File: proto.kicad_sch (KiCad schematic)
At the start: 0 parts

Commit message: update pcb and schematic
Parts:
- added C1, C10, C11, C12, C2, C6: 10uF, Capacitor_SMD:C_0603_1608Metric_Pad1.08x0.95mm_HandSolder, symbol Device:C
- added C13, C14, C15: 0.1uF, Capacitor_SMD:C_0201_0603Metric_Pad0.64x0.40mm_HandSolder, symbol Device:C
- added C3, C8, C9: 4.7uF, Capacitor_SMD:C_0603_1608Metric_Pad1.08x0.95mm_HandSolder, symbol Device:C
- added C4, C5: 220uF, Capacitor_THT:CP_Radial_D10.0mm_P3.80mm, symbol Device:C_Polarized
- added C7: 1uF, Capacitor_SMD:C_0402_1005Metric_Pad0.74x0.62mm_HandSolder, symbol Device:C
- added D1: LED_RGBA, LED_SMD:LED_RGB_Wuerth-PLCC4_3.2x2.8mm_150141M173100, symbol Device:LED_RGBA
- added IC1: WM8960CGEFL_V, WM8960CGEFL_V:QFN50P500X500X100-33N, symbol WM8960CGEFL_V:WM8960CGEFL_V
- added J1: Micro_SD_Card, Connector_Card:microSD_HC_Wuerth_693072010801, symbol Connector:Micro_SD_Card
- added J10: CS, xiao_esp32c3_model:Untitled, symbol Connector:Conn_01x01_Socket
- added J11: BL, xiao_esp32c3_model:Untitled, symbol Connector:Conn_01x01_Socket
- added J12: BAT+, xiao_esp32c3_model:Untitled, symbol Connector:Conn_01x01_Socket
- added J13: BAT-, xiao_esp32c3_model:Untitled, symbol Connector:Conn_01x01_Socket
- added J14: L-, xiao_esp32c3_model:Untitled, symbol Connector:Conn_01x01_Socket
- added J15: L+, xiao_esp32c3_model:Untitled, symbol Connector:Conn_01x01_Socket
- added J16: R-, xiao_esp32c3_model:Untitled, symbol Connector:Conn_01x01_Socket
- added J17: R+, xiao_esp32c3_model:Untitled, symbol Connector:Conn_01x01_Socket
- added J2: AudioJack3, Connector_Audio:Jack_3.5mm_Lumberg_1503_02_Horizontal, symbol Connector_Audio:AudioJack3
- added J3: USB_C_Receptacle_PowerOnly_6P, Connector_USB:USB_C_Receptacle_GCT_USB4125-xx-x-0190_6P_TopMnt_Horizontal, symbol Connector:USB_C_Receptacle_PowerOnly_6P
- added J4: GND, xiao_esp32c3_model:Untitled, symbol Connector:Conn_01x01_Socket
- added J5: VCC, xiao_esp32c3_model:Untitled, symbol Connector:Conn_01x01_Socket
- added J6: SCL, xiao_esp32c3_model:Untitled, symbol Connector:Conn_01x01_Socket
- added J7: SDA, xiao_esp32c3_model:Untitled, symbol Connector:Conn_01x01_Socket
- added J8: RES, xiao_esp32c3_model:Untitled, symbol Connector:Conn_01x01_Socket
- added J9: DC, xiao_esp32c3_model:Untitled, symbol Connector:Conn_01x01_Socket
- added R1, R2: 5.1k, Resistor_SMD:R_0201_0603Metric_Pad0.64x0.40mm_HandSolder, symbol Device:R
- added R3: 2k, Resistor_SMD:R_0201_0603Metric_Pad0.64x0.40mm_HandSolder, symbol Device:R
- added R4: 8k, Resistor_SMD:R_0201_0603Metric_Pad0.64x0.40mm_HandSolder, symbol Device:R
- added R5: 1.5k, Resistor_SMD:R_0201_0603Metric_Pad0.64x0.40mm_HandSolder, symbol Device:R
- added R6, R7, R8, R9: 10k, Resistor_SMD:R_0201_0603Metric_Pad0.64x0.40mm_HandSolder, symbol Device:R
- added SW1, SW2, SW3, SW4, SW5, SW6, SW7, SW8: SW_Push, Button_Switch_THT:SW_PUSH_6mm, symbol Switch:SW_Push
- added TH1: Thermistor, Resistor_SMD:R_0402_1005Metric_Pad0.72x0.64mm_HandSolder, symbol Device:Thermistor
- added U1: (no value), pico2:Raspberrypi pico2 THT, symbol Raspberrypi pico2 W:U
- added U2: BQ24074RGT, Package_DFN_QFN:VQFN-16-1EP_3x3mm_P0.5mm_EP1.6x1.6mm, symbol Battery_Management:BQ24074RGT
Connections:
- new net: J3.A5 (CC1), R2.2
- new net: C4.2, J2.R, R9.2
- new net: IC1.23 (SPK_LN), J14.1 (Pin_1)
- new net: C3.1, IC1.27 (VMID)
- new net: R5.1, U2.12 (ILIM)
- new net: IC1.19 (SPK_RN), J16.1 (Pin_1)
- new net: IC1.22 (SPK_RP), J17.1 (Pin_1)
- new net: IC1.25 (SPK_LP), J15.1 (Pin_1)
- new net: C4.1, IC1.29 (HP_R)
- new net: C5.1, IC1.31 (HP_L)
- new net: C5.2, J2.T, R8.2
- new net: C7.1, J3.A9 (VBUS), J3.B9 (VBUS), U2.13 (IN)
- new net: R4.1, U2.15 (ITERM)
- new net: R3.1, U2.16 (ISET)
- new net: R7.2, U2.7 (~{PGOOD})
- new net: R6.1, U2.9 (~{CHG})
- new net: J3.B5 (CC2), R1.2
- new net +3.3V: C1.1, C10.2, C13.2, C2.1, C6.1, IC1.10 (DBVDD), IC1.32 (AVDD), IC1.8 (DCVDD), J1.4 (VDD), J11.1 (Pin_1), J5.1 (Pin_1), R6.2, R7.1, U1.36 (3V3_OUT), U1.37 (3V3_EN)
- new net +5V: C11.2, C12.2, C14.2, C15.2, IC1.21 (SPKVDD2), IC1.26 (SPKVDD1), U1.40 (VBUS), U2.6 (EN1)
- new net B: D1.3 (BK), U1.29 (GP22)
- new net BAT+: C9.1, J12.1 (Pin_1), U2.2 (BAT), U2.3 (BAT)
- new net BAT-: J13.1 (Pin_1), TH1.1
- new net BLCK: IC1.12 (BCLK), U1.32 (GP27/ADC1/I2C1_SCL)
- new net CS: J1.2 (DAT3/CD), J10.1 (Pin_1), U1.1 (GP0/I2C0_SDA/UART0_TX), U1.17 (GP13/SPI1_CSn/I2C0_SCL/UART0_RX)
- new net DACDAT: IC1.14 (DACDAT), U1.19 (GP14/SPI1_SCK/I2C1_SCL)
- new net DACLRC: IC1.13 (DACLRC), U1.20 (GP15/SPI1_TX/I2C1_SCL)
- new net DC: J9.1 (Pin_1), U1.2 (GP1_/I2C0_SCL/UART0_RX)
- new net G: D1.2 (GK), U1.34 (GP28/ADC2)
- new net GND: C1.2, C10.1, C11.1, C12.1, C13.1, C14.1, C15.1, C2.2, C3.2, C6.2, C7.2, C8.2, C9.2, D1.4 (A), IC1.20 (SPKGND2), IC1.24 (SPKGND1), IC1.28 (AGND), IC1.33 (GND_PADDLE), IC1.9 (DGND), IC1.P$1 (GND_PADDLE), IC1.P$2 (GND_PADDLE), IC1.P$3 (GND_PADDLE), IC1.P$4 (GND_PADDLE), IC1.P$5 (GND_PADDLE), IC1.P$6 (GND_PADDLE), IC1.P$7 (GND_PADDLE), IC1.P$8 (GND_PADDLE), IC1.P$9 (GND_PADDLE), J1.6 (VSS), J1.SH (SHIELD), J2.S, J3.A12 (GND), J3.B12 (GND), J3.SH (SHIELD), J4.1 (Pin_1), R1.1, R2.1, R3.2, R4.2, R5.2, R8.1, R9.1, SW1.2, SW2.2, SW3.2, SW4.2, SW5.2, SW6.2, SW7.2, SW8.2, U1. (SWDIO), U1.13 (GND), U1.18 (GND), U1.23 (GND), U1.28 (GND), U1.3 (GND), U1.33 (GND/AGND), U1.38 (GND), U1.8 (GND), U2.14 (TMR), U2.17 (VSS), U2.4 (~{CE}), U2.5 (EN2), U2.8 (VSS)
- new net MCLK: IC1.11 (MCLK), U1.27 (GP21/I2C0_SCL)
- new net MISO: J1.7 (DAT0), U1.16 (GP12/SPI1_RX/I2C0_SDA/UART0_TX)
- new net MOSI: J1.3 (CMD), U1.15 (GP11/_SPI1_TX/I2C1_SCL)
- new net R: D1.1 (RK), U1.31 (GP26/ADC0/I2C1_SDA)
- new net SCK: J1.5 (CLK), U1.14 (GPI10/SPI1_SCK/I2C1_SDA)
- new net SCL: J6.1 (Pin_1), U1.5 (GP3/SPIO_TX/I2C1SCL)
- new net SCLK: IC1.17 (SCLK), U1.7 (GP5/SPIO_CSn/I2C0_SCL)
- new net SDA: J7.1 (Pin_1), U1.4 (GP2/SPIO_SCK/I2C1_SDA)
- new net SDIN: IC1.18 (SDIN), U1.6 (GP4/SPIO_RX/I2C0_SDA/_UART1_TX)
- new net SW1: SW1.1, U1.9 (GP6/SPIO_SCK/I2C1_SDA)
- new net SW2: SW2.1, U1.10 (GP7/SPI0_TX/_I2C1_SCL)
- new net SW3: SW3.1, U1.11 (GP8/SPI1_RX/I2C0_SDA/UART1_TX)
- new net SW4: SW4.1, U1.12 (GP9/SPI1_CSn/I2C0_SCL/UART1_RX)
- new net SW5: SW5.1, U1.22 (GP17/SPI0_CSn/I2C0_SCL/UART0_RX)
- new net SW6: SW6.1, U1.24 (GP18/SPI0_SCK/I2C1_SDA)
- new net SW7: SW7.1, U1.25 (GP19/SPI0_TX/I2C1_SCL)
- new net SW8: SW8.1, U1.26 (GP20/I2C0_SDA)
- new net TS: TH1.2, U2.1 (TS)
- new net VSYS: C8.1, U1.39 (VSYS), U2.10 (OUT), U2.11 (OUT)
- no-connect marks 0 -> 18

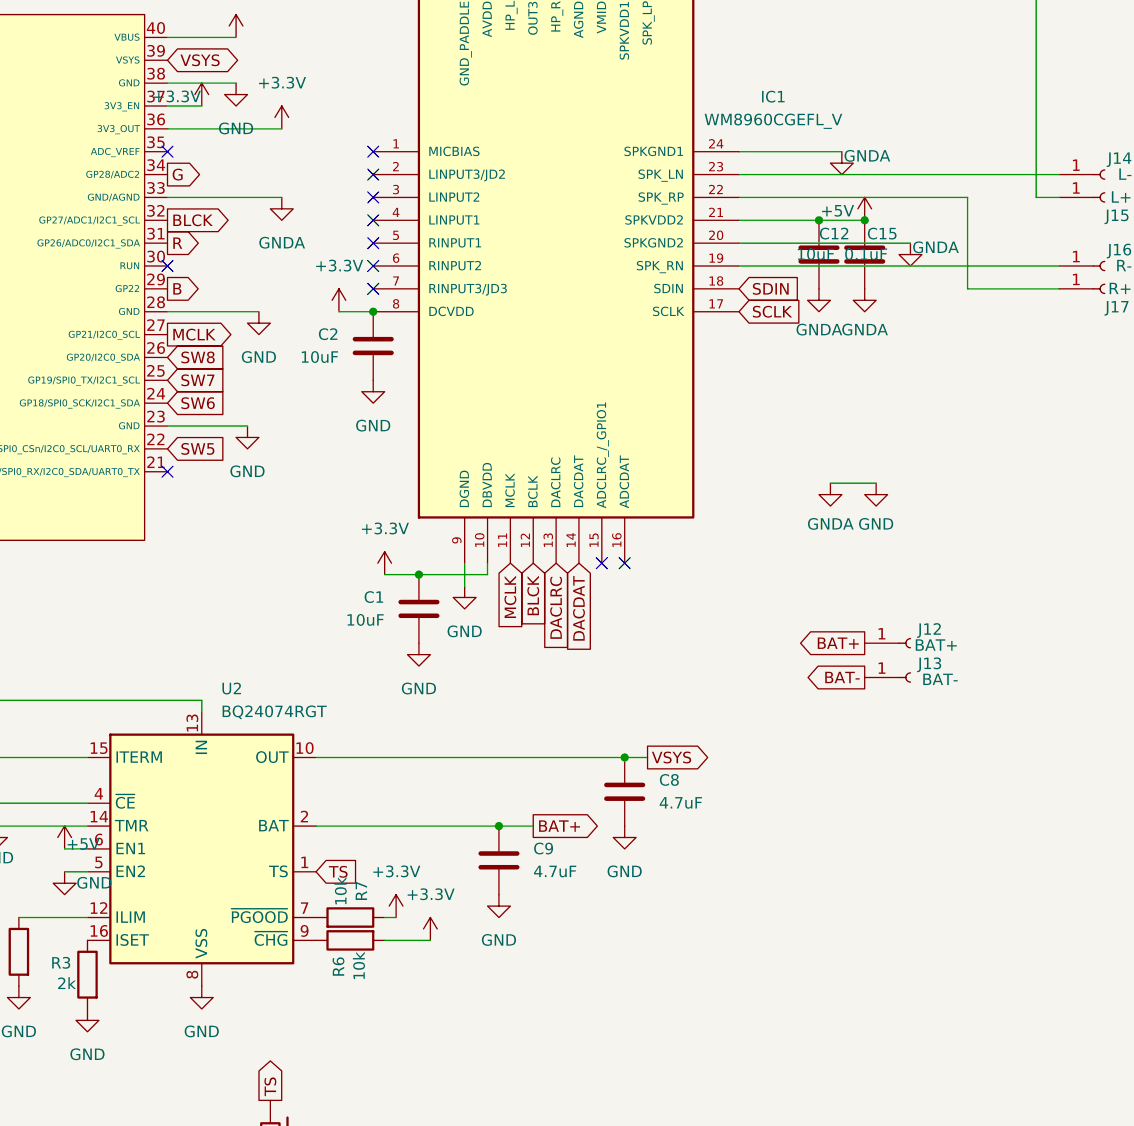
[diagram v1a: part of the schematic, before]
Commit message: Update hardware & software
Added a voltage divider to be able to measure battery level and added very basic firmware
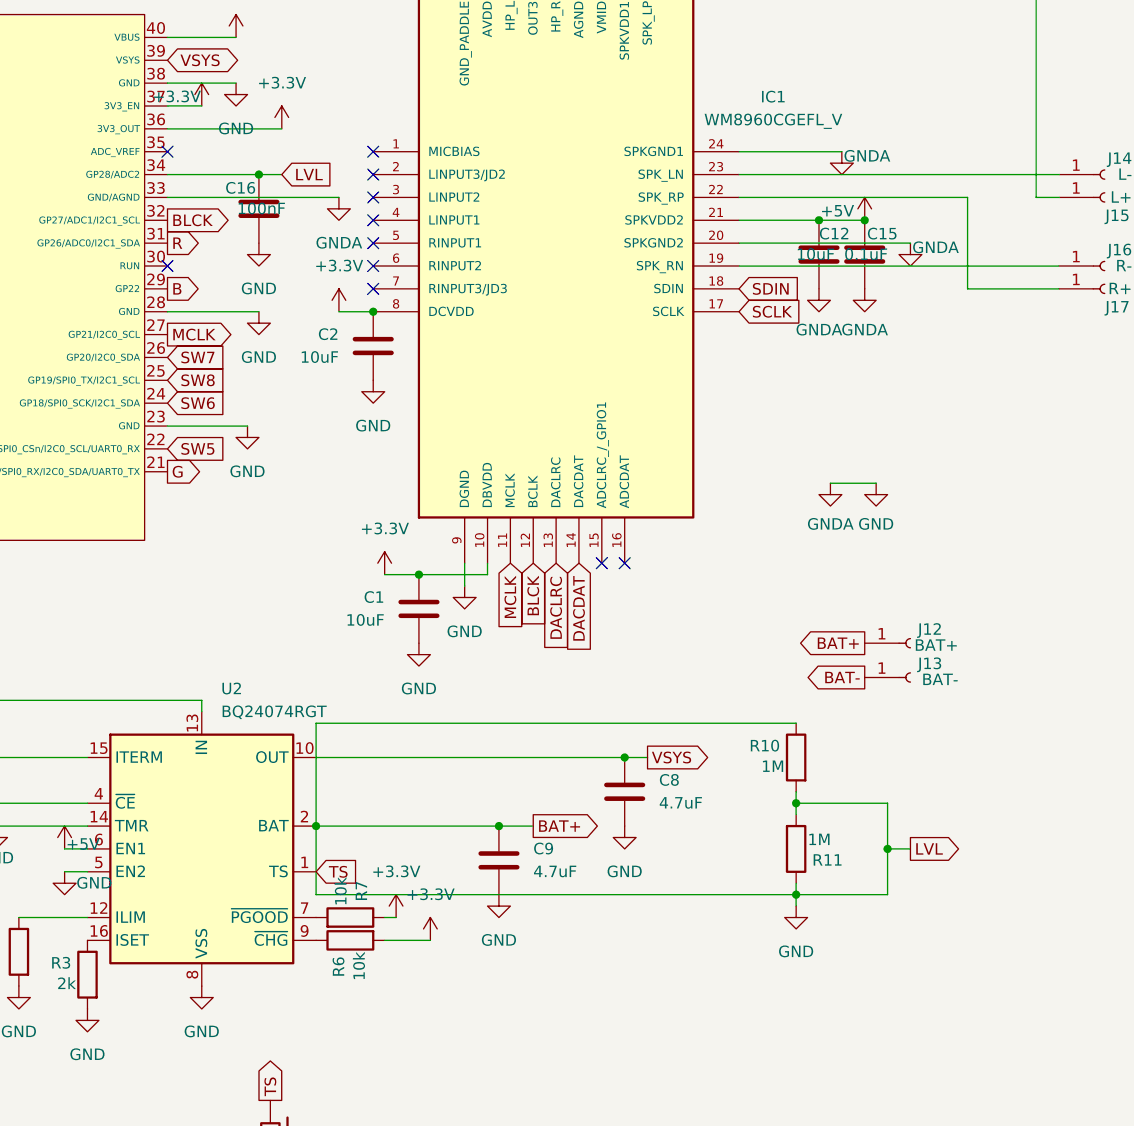
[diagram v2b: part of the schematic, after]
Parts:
- added C16: 100nF, Capacitor_SMD:C_0201_0603Metric_Pad0.64x0.40mm_HandSolder, symbol Device:C
- added R10, R11: 1M, Resistor_SMD:R_0201_0603Metric_Pad0.64x0.40mm_HandSolder, symbol Device:R
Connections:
- net BAT+ is gone; now on net GND: C9.1, J12.1 (Pin_1), U2.2 (BAT), U2.3 (BAT)
- net TS is gone; now on net GND: TH1.2, U2.1 (TS)
- net G: now also U1.21 (GP16/SPI0_RX/I2C0_SDA/UART0_TX); no longer U1.34 (GP28/ADC2)
- net GND: now also U1.34 (GP28/ADC2), C16.1, C16.2, R10.1, R10.2, R11.1, R11.2
- net SW7: now also U1.26 (GP20/I2C0_SDA); no longer U1.25 (GP19/SPI0_TX/I2C1_SCL)
- net SW8: now also U1.25 (GP19/SPI0_TX/I2C1_SCL); no longer U1.26 (GP20/I2C0_SDA)
- no-connect marks 18 -> 17

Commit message: UPDATED stuff again for software + hello world
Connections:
- net BLCK: now also U1.19 (GP14/SPI1_SCK/I2C1_SCL); no longer U1.32 (GP27/ADC1/I2C1_SCL)
- net DACDAT: now also U1.32 (GP27/ADC1/I2C1_SCL); no longer U1.19 (GP14/SPI1_SCK/I2C1_SCL)
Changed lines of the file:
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@@
 	(global_label "BLCK"
 		(shape output)
-		(at 146.05 80.01 0)
-		(fields_autoplaced yes)
-		(effects
-			(font
-				(size 1.27 1.27)
-			)
-			(justify left)
-		)
-		(property "Intersheetrefs" "${INTERSHEET_REFS}"
-			(at 153.8733 80.01 0)
-			(hide yes)
-			(show_name no)
-			(do_not_autoplace no)
-			(effects
-				(font
-					(size 1.27 1.27)
-				)
-				(justify left)
+		(at 97.79 105.41 180)
+		(fields_autoplaced yes)
+		(effects
+			(font
+				(size 1.27 1.27)
+			)
+			(justify right)
+		)
+		(property "Intersheetrefs" "${INTERSHEET_REFS}"
+			(at 89.9667 105.41 0)
+			(hide yes)
+			(show_name no)
+			(do_not_autoplace no)
+			(effects
+				(font
+					(size 1.27 1.27)
+				)
+				(justify right)
 			)
 		)
@@
 		)
 	)
-	(global_label "DACDAT"
-		(shape input)
-		(at 97.79 105.41 180)
-		(fields_autoplaced yes)
-		(effects
-			(font
-				(size 1.27 1.27)
-			)
-			(justify right)
-		)
-		(property "Intersheetrefs" "${INTERSHEET_REFS}"
-			(at 87.85 105.41 0)
-			(hide yes)
-			(show_name no)
-			(do_not_autoplace no)
-			(effects
-				(font
-					(size 1.27 1.27)
-				)
-				(justify right)
-			)
-		)
-	)
 	(global_label "MISO"
 		(shape bidirectional)
@@
 	)
 	(global_label "DACLRC"
-		(shape input)
+		(shape output)
 		(at 97.79 107.95 180)
 		(fields_autoplaced yes)
@@
 			(hide yes)
 			(show_name no)
+			(do_not_autoplace no)
+			(effects
+				(font
+					(size 1.27 1.27)
+				)
+				(justify left)
+			)
+		)
+	)
+	(global_label "DACDAT"
+		(shape output)
+		(at 146.05 80.01 0)
+		(fields_autoplaced yes)
+		(effects
+			(font
+				(size 1.27 1.27)
+			)
+			(justify left)
+		)
+		(property "Intersheetrefs" "${INTERSHEET_REFS}"
+			(at 155.99 80.01 0)
+			(hide yes)
+			(show_name no)
